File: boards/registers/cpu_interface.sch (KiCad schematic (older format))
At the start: 12 parts

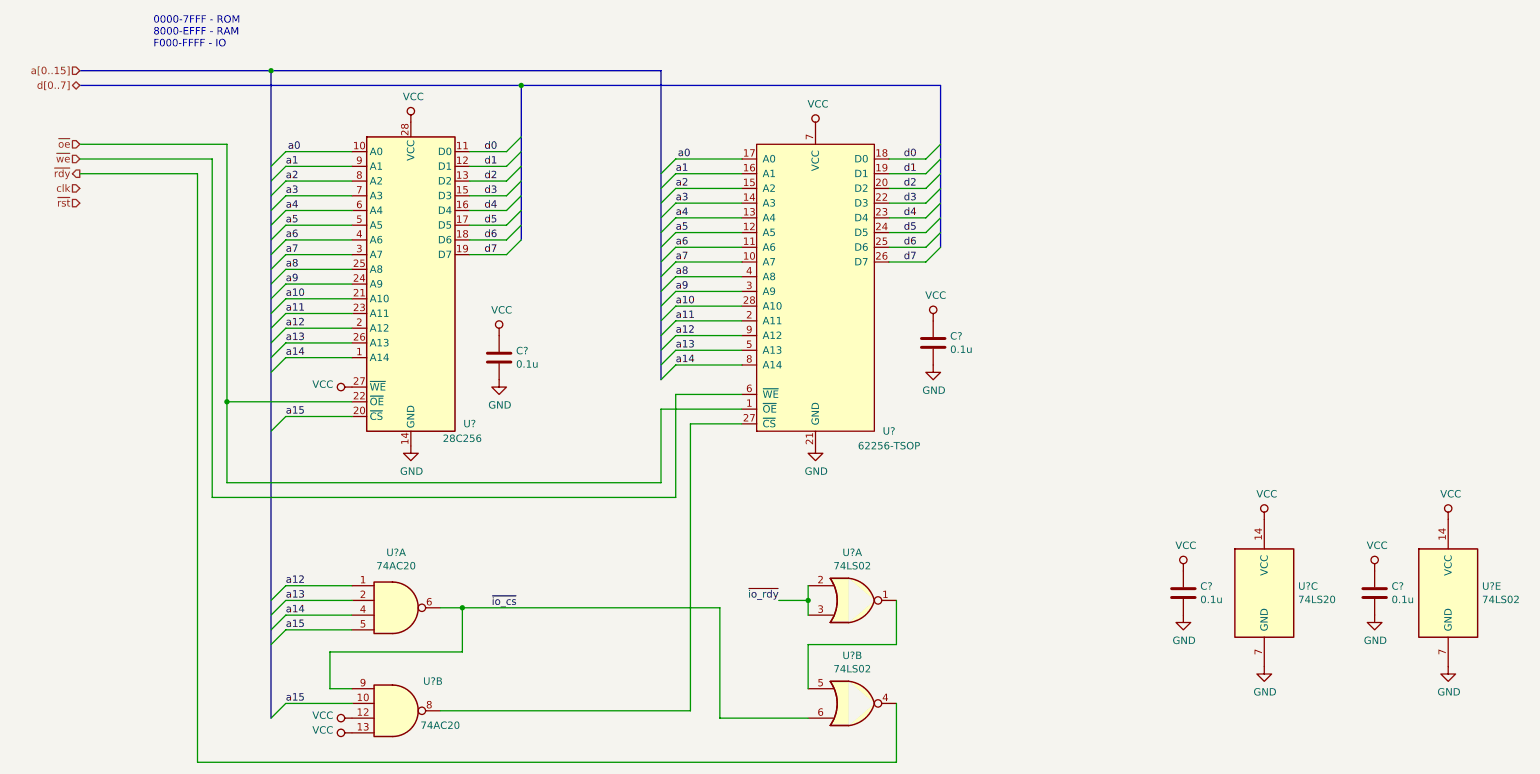
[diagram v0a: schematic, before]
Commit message: IO, ALU, and CU connectors
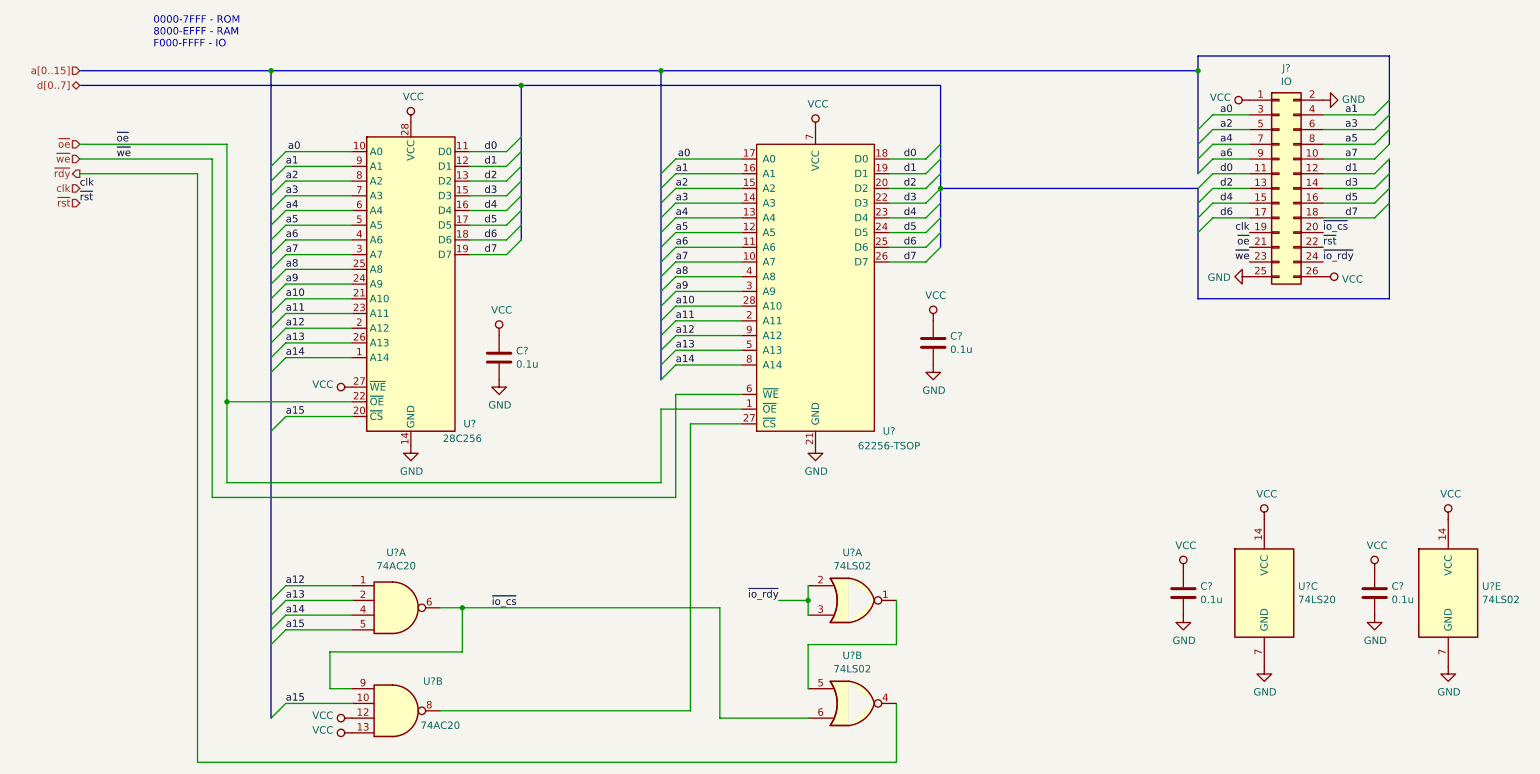
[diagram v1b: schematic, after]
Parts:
- added J?: IO, symbol Connector_Generic:Conn_02x13_Odd_Even
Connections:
- net GND: now also J?.2 (Pin_2), J?.25 (Pin_25)
- net VCC: now also J?.1 (Pin_1), J?.26 (Pin_26)
- net a0: now also J?.3 (Pin_3)
- net a1: now also J?.4 (Pin_4)
- net a2: now also J?.5 (Pin_5)
- net a3: now also J?.6 (Pin_6)
- net a4: now also J?.7 (Pin_7)
- net a5: now also J?.8 (Pin_8)
- net a6: now also J?.9 (Pin_9)
- net a7: now also J?.10 (Pin_10)
- net clk: now also J?.19 (Pin_19)
- net d0: now also J?.11 (Pin_11)
- net d1: now also J?.12 (Pin_12)
- net d2: now also J?.13 (Pin_13)
- net d3: now also J?.14 (Pin_14)
- net d4: now also J?.15 (Pin_15)
- net d5: now also J?.16 (Pin_16)
- net d6: now also J?.17 (Pin_17)
- net d7: now also J?.18 (Pin_18)
- net ~io_cs: now also J?.20 (Pin_20)
- net ~io_rdy: now also J?.24 (Pin_24)
- net ~oe: now also J?.21 (Pin_21)
- net ~rst: now also J?.22 (Pin_22)
- net ~we: now also J?.23 (Pin_23)
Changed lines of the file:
@@
 Wire Wire Line
 	7050 5900 7050 5500
-Wire Bus Line
-	4500 1300 4500 2350
-Wire Bus Line
-	7350 1300 7350 2400
-Wire Bus Line
-	5450 1200 5450 3300
-Wire Bus Line
-	2800 1200 2800 5600
 $Comp
 L power:VCC #PWR?
@@
 	0    -1   -1   0
 $EndComp
+$Comp
+L power:GND #PWR?
+U 1 1 5EDD5828
+P 9950 1400
+F 0 "#PWR?" H 9950 1150 50  0001 C CNN
+F 1 "GND" V 9955 1272 50  0000 R CNN
+F 2 "" H 9950 1400 50  0001 C CNN
+F 3 "" H 9950 1400 50  0001 C CNN
+	1    9950 1400
+	0    -1   -1   0
+$EndComp
+$Comp
+L power:GND #PWR?
+U 1 1 5EDD64B3
+P 9450 2600
+F 0 "#PWR?" H 9450 2350 50  0001 C CNN
+F 1 "GND" V 9455 2472 50  0000 R CNN
+F 2 "" H 9450 2600 50  0001 C CNN
+F 3 "" H 9450 2600 50  0001 C CNN
+	1    9450 2600
+	0    1    1    0
+$EndComp
+$Comp
+L power:VCC #PWR?
+U 1 1 5EDD71B4
+P 9450 1400
+F 0 "#PWR?" H 9450 1250 50  0001 C CNN
+F 1 "VCC" V 9468 1527 50  0000 L CNN
+F 2 "" H 9450 1400 50  0001 C CNN
+F 3 "" H 9450 1400 50  0001 C CNN
+	1    9450 1400
+	0    -1   -1   0
+$EndComp
+$Comp
+L power:VCC #PWR?
+U 1 1 5EDD7F36
+P 9950 2600
+F 0 "#PWR?" H 9950 2450 50  0001 C CNN
+F 1 "VCC" V 9967 2728 50  0000 L CNN
+F 2 "" H 9950 2600 50  0001 C CNN
+F 3 "" H 9950 2600 50  0001 C CNN
+	1    9950 2600
+	0    1    1    0
+$EndComp
+Text Label 9950 2500 0    50   ~ 0
+~io_rdy
+Text Label 9950 2300 0    50   ~ 0
+~io_cs
+Text Label 1750 1800 0    50   ~ 0
+~we
+Text Label 1750 1700 0    50   ~ 0
+~oe
+Text Label 1500 2000 0    50   ~ 0
+clk
+Text Label 1500 2100 0    50   ~ 0
+~rst
+Text Label 9450 2400 2    50   ~ 0
+~oe
+Text Label 9450 2500 2    50   ~ 0
+~we
+Text Label 9950 2400 0    50   ~ 0
+~rst
+Text Label 9450 2300 2    50   ~ 0
+clk
+Entry Wire Line
+	10300 1600 10400 1500
+Entry Wire Line
+	10300 1500 10400 1400
+Wire Wire Line
+	9950 1500 10300 1500
+Wire Wire Line
+	10300 1600 9950 1600
+Entry Wire Line
+	10300 1800 10400 1700
+Entry Wire Line
+	10300 1700 10400 1600
+Wire Wire Line
+	9950 1700 10300 1700
+Wire Wire Line
+	10300 1800 9950 1800
+Entry Wire Line
+	9100 1600 9200 1500
+Entry Wire Line
+	9100 1700 9200 1600
+Wire Wire Line
+	9450 1500 9200 1500
+Wire Wire Line
+	9200 1600 9450 1600
+Entry Wire Line
+	9100 1800 9200 1700
+Entry Wire Line
+	9100 1900 9200 1800
+Wire Wire Line
+	9450 1700 9200 1700
+Wire Wire Line
+	9200 1800 9450 1800
+Text Label 9250 1500 0    50   ~ 0
+a0
+Text Label 9250 1600 0    50   ~ 0
+a2
+Text Label 9250 1700 0    50   ~ 0
+a4
+Text Label 9250 1800 0    50   ~ 0
+a6
+Text Label 10100 1500 0    50   ~ 0
+a1
+Text Label 10100 1600 0    50   ~ 0
+a3
+Text Label 10100 1700 0    50   ~ 0
+a5
+Text Label 10100 1800 0    50   ~ 0
+a7
+$Comp
+L Connector_Generic:Conn_02x13_Odd_Even J?
+U 1 1 5EEDDD9A
+P 9650 2000
+F 0 "J?" H 9700 2817 50  0000 C CNN
+F 1 "IO" H 9700 2726 50  0000 C CNN
+F 2 "" H 9650 2000 50  0001 C CNN
+F 3 "~" H 9650 2000 50  0001 C CNN
+	1    9650 2000
+	1    0    0    -1
+$EndComp
+Text Label 10100 2200 0    50   ~ 0
+d7
+Text Label 10100 2100 0    50   ~ 0
+d5
+Text Label 10100 2000 0    50   ~ 0
+d3
+Text Label 10100 1900 0    50   ~ 0
+d1
+Wire Wire Line
+	9950 1900 10300 1900
+Wire Wire Line
+	10300 2000 9950 2000
+Wire Wire Line
+	9950 2100 10300 2100
+Wire Wire Line
+	10300 2200 9950 2200
+Entry Wire Line
+	10300 2200 10400 2100
+Entry Wire Line
+	10300 2100 10400 2000
+Entry Wire Line
+	10300 2000 10400 1900
+Entry Wire Line
+	10300 1900 10400 1800
+Text Label 9250 2200 0    50   ~ 0
+d6
+Text Label 9250 2100 0    50   ~ 0
+d4
+Text Label 9250 2000 0    50   ~ 0
+d2
+Text Label 9250 1900 0    50   ~ 0
+d0
+Wire Wire Line
+	9200 2200 9450 2200
+Wire Wire Line
+	9450 2100 9200 2100
+Wire Wire Line
+	9200 2000 9450 2000
+Wire Wire Line
+	9450 1900 9200 1900
+Entry Wire Line
+	9100 2000 9200 1900
+Entry Wire Line
+	9100 2100 9200 2000
+Entry Wire Line
+	9100 2200 9200 2100
+Entry Wire Line
+	9100 2300 9200 2200
+Wire Bus Line
+	10400 1100 9100 1100
+Wire Bus Line
+	5450 1200 9100 1200
+Wire Bus Line
+	9100 1100 9100 1200
+Connection ~ 5450 1200
+Connection ~ 9100 1200
+Wire Bus Line
+	10400 2750 9100 2750
+Wire Bus Line
+	9100 2000 7350 2000
+Wire Bus Line
+	10400 1100 10400 1700
+Wire Bus Line
+	7350 1300 7350 2000
+Wire Bus Line
+	9100 1200 9100 1900
+Wire Bus Line
+	10400 1800 10400 2750
+Wire Bus Line
+	9100 2000 9100 2750
+Wire Bus Line
+	7350 2000 7350 2400
+Wire Bus Line
+	4500 1300 4500 2350
+Wire Bus Line
+	5450 1200 5450 3300
+Wire Bus Line
+	2800 1200 2800 5600
+Connection ~ 7350 2000
 $EndSCHEMATC

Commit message: Fix unconnected nets
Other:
- moved on the sheet: C?, U?C, U?E
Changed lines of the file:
@@
 L 74xx:74LS20 U?
 U 3 1 5ECCA4CA
-P 9550 4750
-F 0 "U?" H 9780 4796 50  0000 L CNN
-F 1 "74LS20" H 9780 4705 50  0000 L CNN
-F 2 "" H 9550 4750 50  0001 C CNN
-F 3 "http://www.ti.com/lit/gpn/sn74LS20" H 9550 4750 50  0001 C CNN
-	3    9550 4750
+P 9050 4800
+F 0 "U?" H 9280 4846 50  0000 L CNN
+F 1 "74LS20" H 9280 4755 50  0000 L CNN
+F 2 "" H 9050 4800 50  0001 C CNN
+F 3 "http://www.ti.com/lit/gpn/sn74LS20" H 9050 4800 50  0001 C CNN
+	3    9050 4800
 	1    0    0    -1
 $EndComp
@@
 L power:GND #PWR?
 U 1 1 5ECCC6F9
-P 9550 5250
-F 0 "#PWR?" H 9550 5000 50  0001 C CNN
-F 1 "GND" H 9555 5077 50  0000 C CNN
-F 2 "" H 9550 5250 50  0001 C CNN
-F 3 "" H 9550 5250 50  0001 C CNN
-	1    9550 5250
+P 9050 5300
+F 0 "#PWR?" H 9050 5050 50  0001 C CNN
+F 1 "GND" H 9055 5127 50  0000 C CNN
+F 2 "" H 9050 5300 50  0001 C CNN
+F 3 "" H 9050 5300 50  0001 C CNN
+	1    9050 5300
 	1    0    0    -1
 $EndComp
@@
 L power:VCC #PWR?
 U 1 1 5ECCCCC9
-P 9550 4250
-F 0 "#PWR?" H 9550 4100 50  0001 C CNN
-F 1 "VCC" H 9567 4423 50  0000 C CNN
-F 2 "" H 9550 4250 50  0001 C CNN
-F 3 "" H 9550 4250 50  0001 C CNN
-	1    9550 4250
+P 9050 4300
+F 0 "#PWR?" H 9050 4150 50  0001 C CNN
+F 1 "VCC" H 9067 4473 50  0000 C CNN
+F 2 "" H 9050 4300 50  0001 C CNN
+F 3 "" H 9050 4300 50  0001 C CNN
+	1    9050 4300
 	1    0    0    -1
 $EndComp
@@
 L Device:C C?
 U 1 1 5ECDA802
-P 9000 4750
-F 0 "C?" H 9115 4796 50  0000 L CNN
-F 1 "0.1u" H 9115 4705 50  0000 L CNN
-F 2 "" H 9038 4600 50  0001 C CNN
-F 3 "~" H 9000 4750 50  0001 C CNN
-	1    9000 4750
+P 8500 4800
+F 0 "C?" H 8615 4846 50  0000 L CNN
+F 1 "0.1u" H 8615 4755 50  0000 L CNN
+F 2 "" H 8538 4650 50  0001 C CNN
+F 3 "~" H 8500 4800 50  0001 C CNN
+	1    8500 4800
 	1    0    0    -1
 $EndComp
@@
 L power:VCC #PWR?
 U 1 1 5ECDA808
-P 9000 4600
-F 0 "#PWR?" H 9000 4450 50  0001 C CNN
-F 1 "VCC" H 9017 4773 50  0000 C CNN
-F 2 "" H 9000 4600 50  0001 C CNN
-F 3 "" H 9000 4600 50  0001 C CNN
-	1    9000 4600
+P 8500 4650
+F 0 "#PWR?" H 8500 4500 50  0001 C CNN
+F 1 "VCC" H 8517 4823 50  0000 C CNN
+F 2 "" H 8500 4650 50  0001 C CNN
+F 3 "" H 8500 4650 50  0001 C CNN
+	1    8500 4650
 	1    0    0    -1
 $EndComp
@@
 L power:GND #PWR?
 U 1 1 5ECDA80E
-P 9000 4900
-F 0 "#PWR?" H 9000 4650 50  0001 C CNN
-F 1 "GND" H 9005 4727 50  0000 C CNN
-F 2 "" H 9000 4900 50  0001 C CNN
-F 3 "" H 9000 4900 50  0001 C CNN
-	1    9000 4900
+P 8500 4950
+F 0 "#PWR?" H 8500 4700 50  0001 C CNN
+F 1 "GND" H 8505 4777 50  0000 C CNN
+F 2 "" H 8500 4950 50  0001 C CNN
+F 3 "" H 8500 4950 50  0001 C CNN
+	1    8500 4950
 	1    0    0    -1
 $EndComp
@@
 L 74xx:74LS02 U?
 U 5 1 5ECEB0A9
-P 10800 4750
-F 0 "U?" H 11030 4796 50  0000 L CNN
-F 1 "74LS02" H 11030 4705 50  0000 L CNN
-F 2 "" H 10800 4750 50  0001 C CNN
-F 3 "http://www.ti.com/lit/gpn/sn74ls02" H 10800 4750 50  0001 C CNN
-	5    10800 4750
+P 10300 4800
+F 0 "U?" H 10530 4846 50  0000 L CNN
+F 1 "74LS02" H 10530 4755 50  0000 L CNN
+F 2 "" H 10300 4800 50  0001 C CNN
+F 3 "http://www.ti.com/lit/gpn/sn74ls02" H 10300 4800 50  0001 C CNN
+	5    10300 4800
 	1    0    0    -1
 $EndComp
@@
 L power:VCC #PWR?
 U 1 1 5ECEF161
-P 10800 4250
-F 0 "#PWR?" H 10800 4100 50  0001 C CNN
-F 1 "VCC" H 10817 4423 50  0000 C CNN
-F 2 "" H 10800 4250 50  0001 C CNN
-F 3 "" H 10800 4250 50  0001 C CNN
-	1    10800 4250
+P 10300 4300
+F 0 "#PWR?" H 10300 4150 50  0001 C CNN
+F 1 "VCC" H 10317 4473 50  0000 C CNN
+F 2 "" H 10300 4300 50  0001 C CNN
+F 3 "" H 10300 4300 50  0001 C CNN
+	1    10300 4300
 	1    0    0    -1
 $EndComp
@@
 L power:GND #PWR?
 U 1 1 5ECEF827
-P 10800 5250
-F 0 "#PWR?" H 10800 5000 50  0001 C CNN
-F 1 "GND" H 10805 5077 50  0000 C CNN
-F 2 "" H 10800 5250 50  0001 C CNN
-F 3 "" H 10800 5250 50  0001 C CNN
-	1    10800 5250
+P 10300 5300
+F 0 "#PWR?" H 10300 5050 50  0001 C CNN
+F 1 "GND" H 10305 5127 50  0000 C CNN
+F 2 "" H 10300 5300 50  0001 C CNN
+F 3 "" H 10300 5300 50  0001 C CNN
+	1    10300 5300
 	1    0    0    -1
 $EndComp
@@
 L Device:C C?
 U 1 1 5ECF04C3
-P 10300 4750
-F 0 "C?" H 10415 4796 50  0000 L CNN
-F 1 "0.1u" H 10415 4705 50  0000 L CNN
-F 2 "" H 10338 4600 50  0001 C CNN
-F 3 "~" H 10300 4750 50  0001 C CNN
-	1    10300 4750
+P 9800 4800
+F 0 "C?" H 9915 4846 50  0000 L CNN
+F 1 "0.1u" H 9915 4755 50  0000 L CNN
+F 2 "" H 9838 4650 50  0001 C CNN
+F 3 "~" H 9800 4800 50  0001 C CNN
+	1    9800 4800
 	1    0    0    -1
 $EndComp
@@
 L power:VCC #PWR?
 U 1 1 5ECF04C9
-P 10300 4600
-F 0 "#PWR?" H 10300 4450 50  0001 C CNN
-F 1 "VCC" H 10317 4773 50  0000 C CNN
-F 2 "" H 10300 4600 50  0001 C CNN
-F 3 "" H 10300 4600 50  0001 C CNN
-	1    10300 4600
+P 9800 4650
+F 0 "#PWR?" H 9800 4500 50  0001 C CNN
+F 1 "VCC" H 9817 4823 50  0000 C CNN
+F 2 "" H 9800 4650 50  0001 C CNN
+F 3 "" H 9800 4650 50  0001 C CNN
+	1    9800 4650
 	1    0    0    -1
 $EndComp
@@
 L power:GND #PWR?
 U 1 1 5ECF04CF
-P 10300 4900
-F 0 "#PWR?" H 10300 4650 50  0001 C CNN
-F 1 "GND" H 10305 4727 50  0000 C CNN
-F 2 "" H 10300 4900 50  0001 C CNN
-F 3 "" H 10300 4900 50  0001 C CNN
-	1    10300 4900
+P 9800 4950
+F 0 "#PWR?" H 9800 4700 50  0001 C CNN
+F 1 "GND" H 9805 4777 50  0000 C CNN
+F 2 "" H 9800 4950 50  0001 C CNN
+F 3 "" H 9800 4950 50  0001 C CNN
+	1    9800 4950
 	1    0    0    -1
 $EndComp
@@
 Wire Bus Line
 	9100 2000 7350 2000
+Connection ~ 7350 2000
 Wire Bus Line
 	10400 1100 10400 1700
@@
 Wire Bus Line
 	2800 1200 2800 5600
-Connection ~ 7350 2000
 $EndSCHEMATC

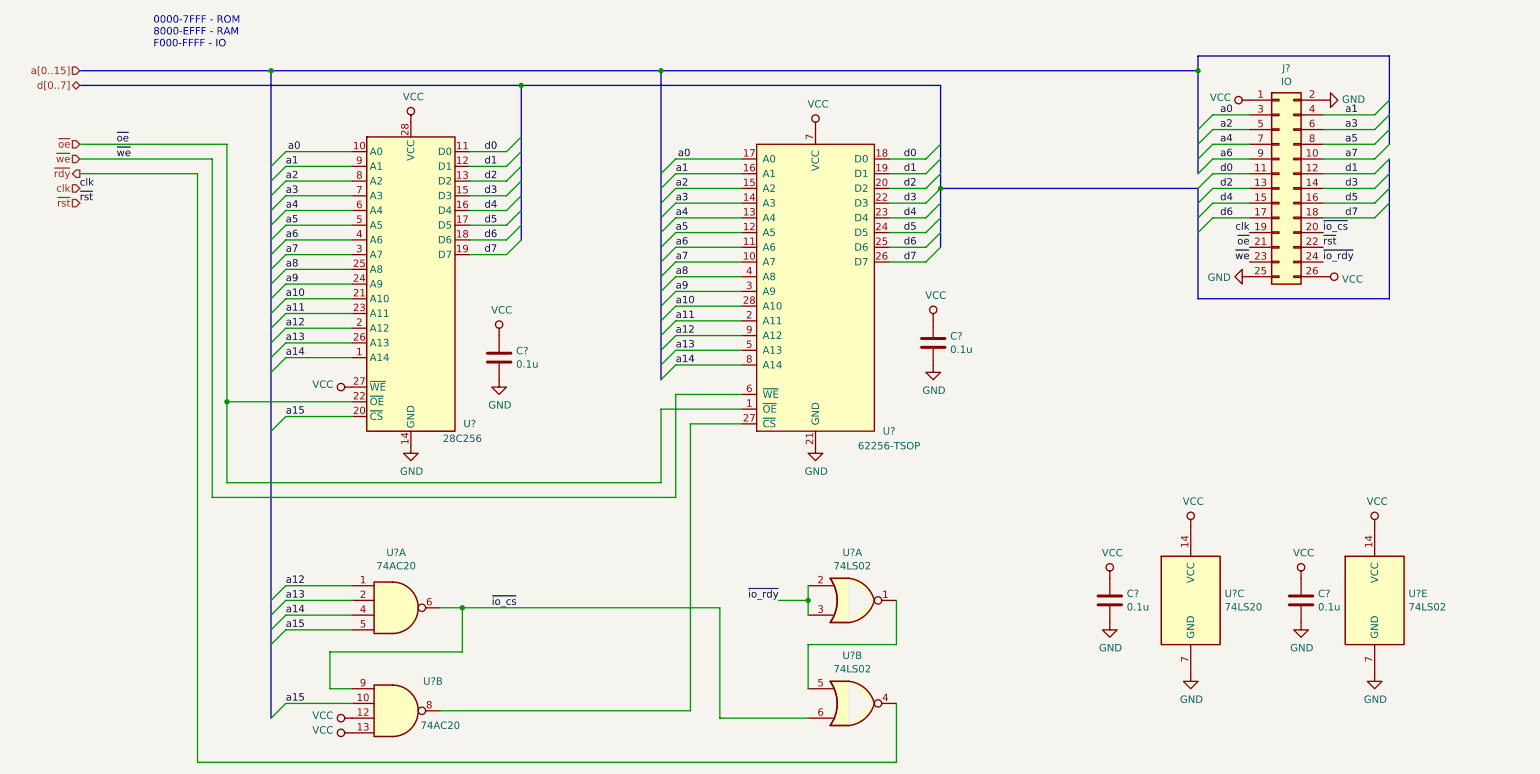
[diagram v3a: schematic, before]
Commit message: Annotated schematics, assigned footprints
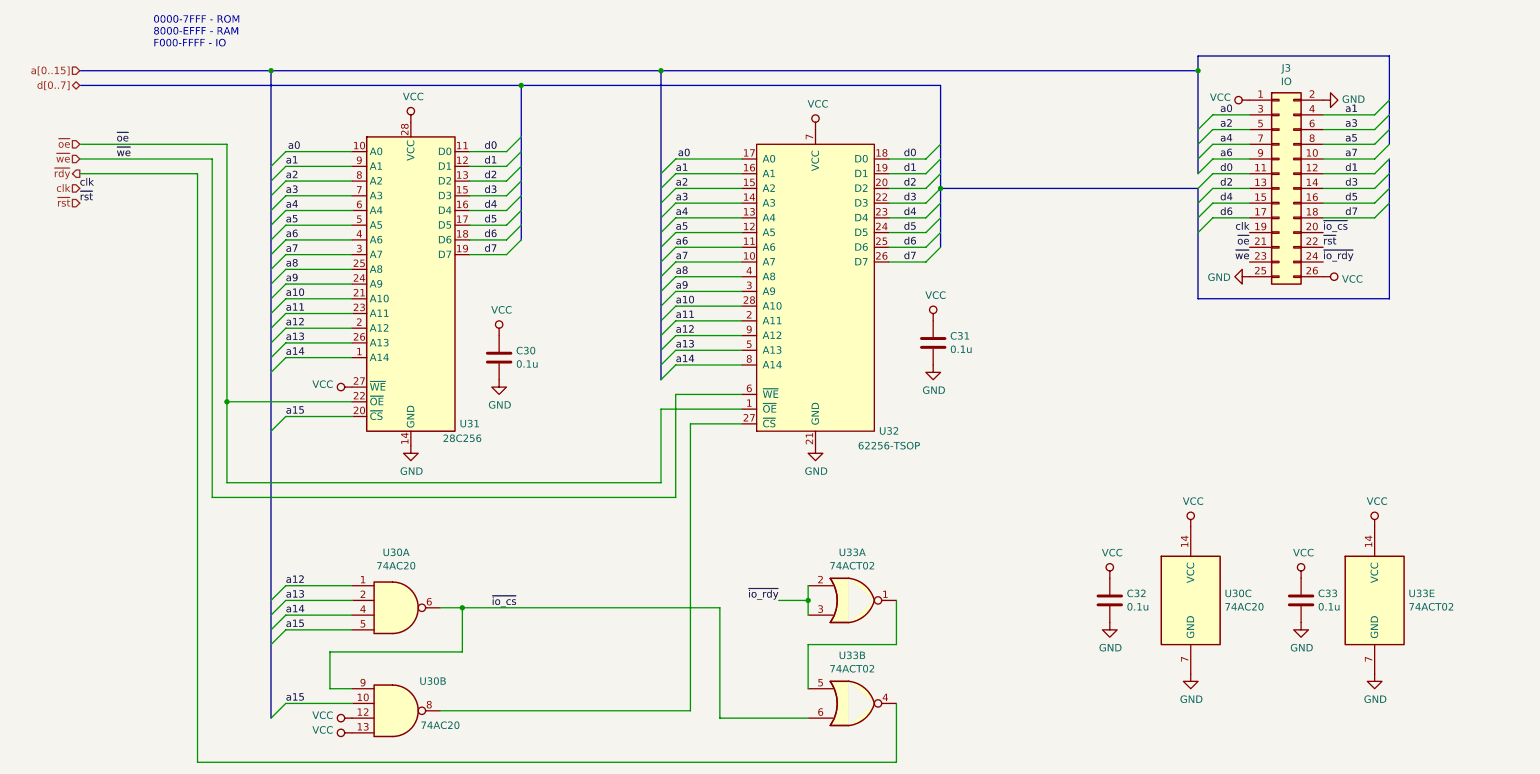
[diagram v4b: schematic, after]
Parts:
- C30, C31, C32, C33: renamed from C?; footprint (none) -> Capacitor_SMD:C_0805_2012Metric
- J3: renamed from J?; footprint (none) -> Connector_PinSocket_2.54mm:PinSocket_2x13_P2.54mm_Horizontal
- U30: renamed from U?; footprint (none) -> Package_SO:SOIC-14_3.9x8.7mm_P1.27mm
- U30: renamed from U?; value 74LS20 -> 74AC20; footprint (none) -> Package_SO:SOIC-14_3.9x8.7mm_P1.27mm
- U31: renamed from U?; footprint (none) -> Package_LCC:PLCC-28_SMD-Socket
- U33: renamed from U?; value 74LS02 -> 74ACT02; footprint (none) -> Package_SO:TSSOP-14_4.4x5mm_P0.65mm
- gave numbers to parts that had none: 1
